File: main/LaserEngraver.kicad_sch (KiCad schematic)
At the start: 3 parts, among them J1 Conn_01x04_Socket, U1 STM32F103C8Tx

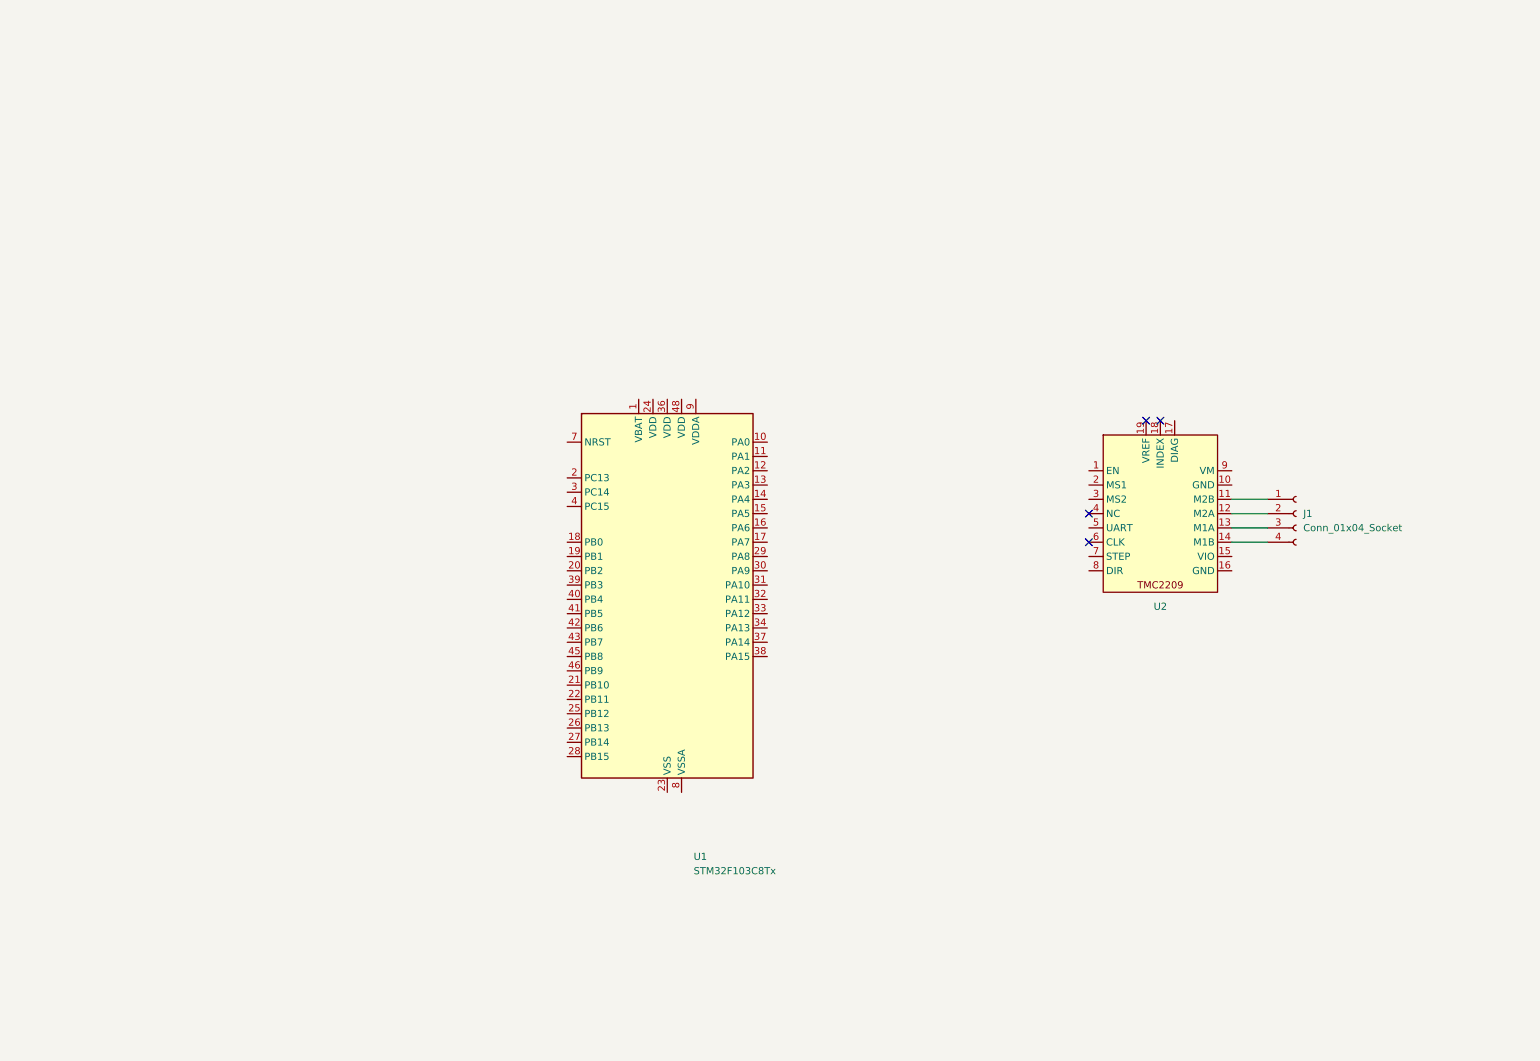
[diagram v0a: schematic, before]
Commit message: Made most connections between STM32 and motor drivers, as well as onboard connectors
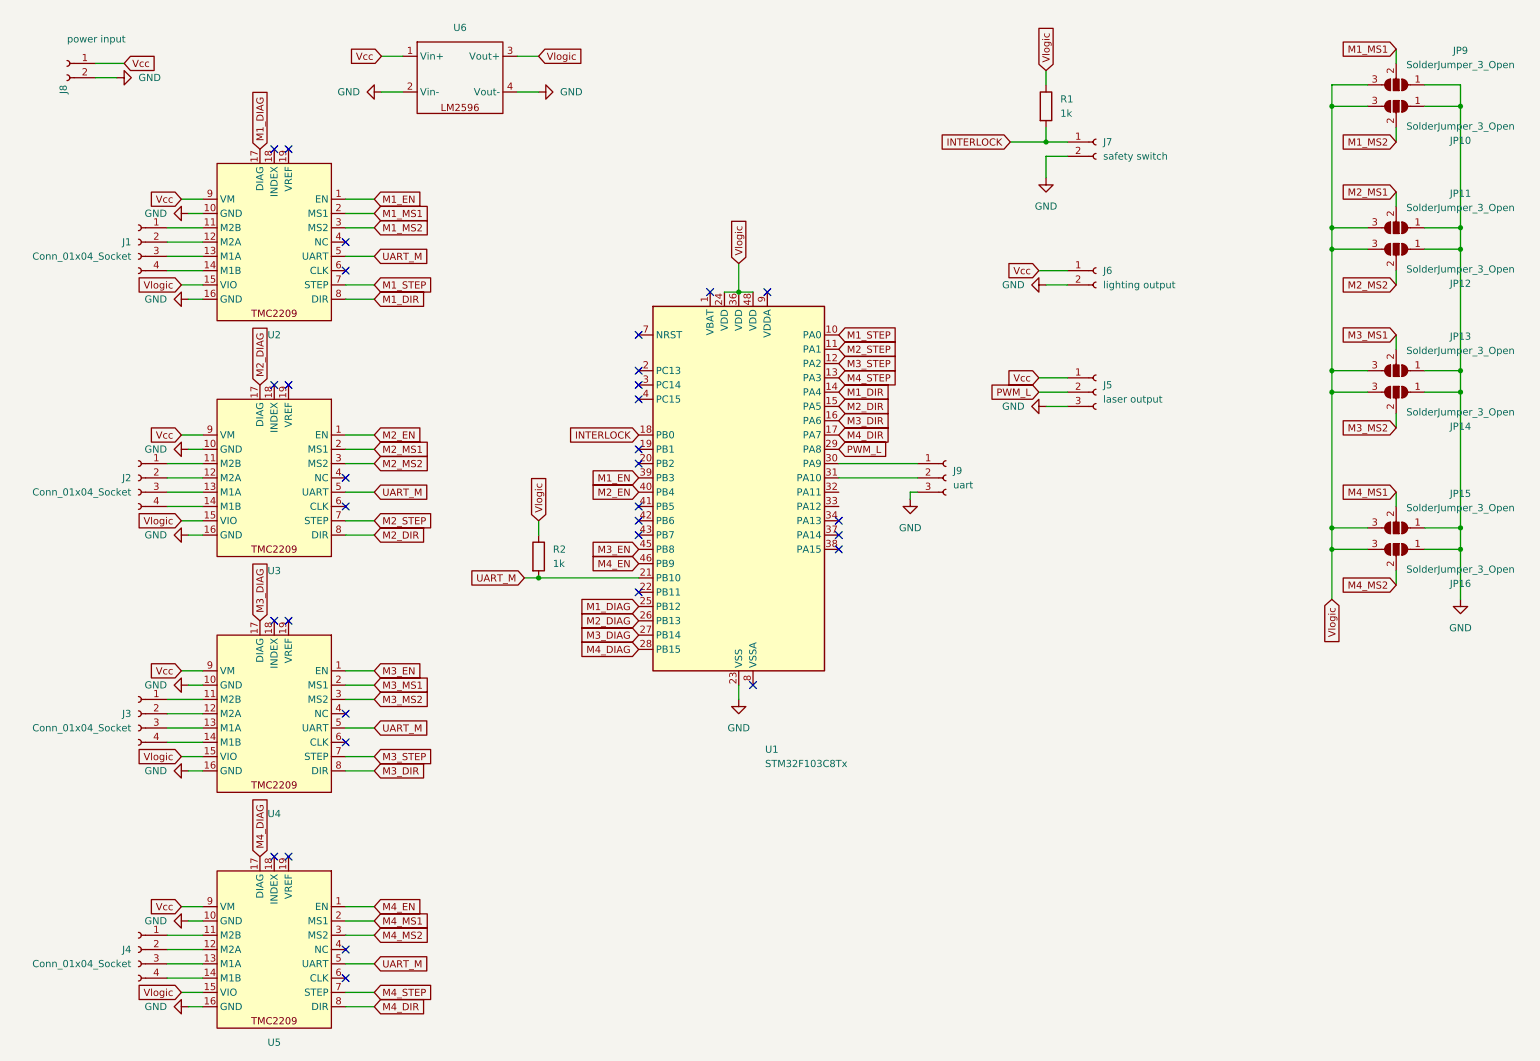
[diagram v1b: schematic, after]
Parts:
- added J2, J3, J4: Conn_01x04_Socket, symbol Connector:Conn_01x04_Socket
- added J5: laser output, symbol Connector:Conn_01x03_Socket
- added J6: lighting output, symbol Connector:Conn_01x02_Socket
- added J7: safety switch, symbol Connector:Conn_01x02_Socket
- added J8: power input, symbol Connector:Conn_01x02_Socket
- added J9: uart, symbol Connector:Conn_01x03_Socket
- added JP10, JP11, JP12, JP13, JP14, JP15, JP16, JP9: SolderJumper_3_Open, symbol Jumper:SolderJumper_3_Open
- added R1, R2: 1k, symbol Device:R
- added U3, U4, U5: (no value), symbol CustomSymbols:TMC2209
- added U6: (no value), symbol CustomSymbols:buck_converter_lm2596
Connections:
- net M1_EN: now reaches U2.1 (EN)
- net M1_EN: now also U1.39 (PB3)
- net GND: now reaches U2.10 (GND)
- net GND: now also U1.23 (VSS), U1.35 (VSS), U1.47 (VSS), U2.16 (GND), J5.3 (Pin_3), J6.2 (Pin_2), J7.2 (Pin_2), J8.2 (Pin_2), J9.3 (Pin_3), JP10.1 (A), JP11.1 (A), JP12.1 (A), JP13.1 (A), JP14.1 (A), JP15.1 (A), JP16.1 (A), JP9.1 (A), U3.10 (GND), U3.16 (GND), U4.10 (GND), U4.16 (GND), U5.10 (GND), U5.16 (GND), U6.2 (Vin-), U6.4 (Vout-)
- net Vlogic: now reaches U2.15 (VIO)
- net Vlogic: now also U1.24 (VDD), U1.36 (VDD), U1.48 (VDD), JP10.3 (B), JP11.3 (B), JP12.3 (B), JP13.3 (B), JP14.3 (B), JP15.3 (B), JP16.3 (B), JP9.3 (B), R1.1, R2.1, U3.15 (VIO), U4.15 (VIO), U5.15 (VIO), U6.3 (Vout+)
- net M1_DIAG: now reaches U2.17 (DIAG)
- net M1_DIAG: now also U1.25 (PB12)
- net M1_MS1: now reaches U2.2 (MS1)
- net M1_MS1: now also JP9.2 (C)
- net M1_MS2: now reaches U2.3 (MS2)
- net M1_MS2: now also JP10.2 (C)
- net UART_M: now reaches U2.5 (UART)
- net UART_M: now also U1.21 (PB10), R2.2, U3.5 (UART), U4.5 (UART), U5.5 (UART)
- net M1_STEP: now reaches U2.7 (STEP)
- net M1_STEP: now also U1.10 (PA0)
- net M1_DIR: now reaches U2.8 (DIR)
- net M1_DIR: now also U1.14 (PA4)
- net Vcc: now reaches U2.9 (VM)
- net Vcc: now also J5.1 (Pin_1), J6.1 (Pin_1), J8.1 (Pin_1), U3.9 (VM), U4.9 (VM), U5.9 (VM), U6.1 (Vin+)
- net M2_STEP: now reaches U1.11 (PA1)
- net M2_STEP: now also U3.7 (STEP)
- net M3_STEP: now reaches U1.12 (PA2)
- net M3_STEP: now also U4.7 (STEP)
- net M4_STEP: now reaches U1.13 (PA3)
- net M4_STEP: now also U5.7 (STEP)
- net M2_DIR: now reaches U1.15 (PA5)
- net M2_DIR: now also U3.8 (DIR)
- net M3_DIR: now reaches U1.16 (PA6)
- net M3_DIR: now also U4.8 (DIR)
- net M4_DIR: now reaches U1.17 (PA7)
- net M4_DIR: now also U5.8 (DIR)
- net INTERLOCK: now reaches U1.18 (PB0)
- net INTERLOCK: now also J7.1 (Pin_1), R1.2
- net M2_DIAG: now reaches U1.26 (PB13)
- net M2_DIAG: now also U3.17 (DIAG)
- net M3_DIAG: now reaches U1.27 (PB14)
- net M3_DIAG: now also U4.17 (DIAG)
- net M4_DIAG: now reaches U1.28 (PB15)
- net M4_DIAG: now also U5.17 (DIAG)
- net PWM_L: now reaches U1.29 (PA8)
- net PWM_L: now also J5.2 (Pin_2)
- net at U1.30 (PA9): now also J9.1 (Pin_1)
- net at U1.31 (PA10): now also J9.2 (Pin_2)
- net M2_EN: now reaches U1.40 (PB4)
- net M2_EN: now also U3.1 (EN)
- net M3_EN: now reaches U1.45 (PB8)
- net M3_EN: now also U4.1 (EN)
- net M4_EN: now reaches U1.46 (PB9)
- net M4_EN: now also U5.1 (EN)
- new net: J3.1 (Pin_1), U4.11 (M2B)
- new net: J3.2 (Pin_2), U4.12 (M2A)
- new net: J3.3 (Pin_3), U4.13 (M1A)
- new net: J3.4 (Pin_4), U4.14 (M1B)
- new net: J2.1 (Pin_1), U3.11 (M2B)
- new net: J2.2 (Pin_2), U3.12 (M2A)
- new net: J2.3 (Pin_3), U3.13 (M1A)
- new net: J2.4 (Pin_4), U3.14 (M1B)
- new net: J4.1 (Pin_1), U5.11 (M2B)
- new net: J4.2 (Pin_2), U5.12 (M2A)
- new net: J4.3 (Pin_3), U5.13 (M1A)
- new net: J4.4 (Pin_4), U5.14 (M1B)
- new net M2_MS1: JP11.2 (C), U3.2 (MS1)
- new net M2_MS2: JP12.2 (C), U3.3 (MS2)
- new net M3_MS1: JP13.2 (C), U4.2 (MS1)
- new net M3_MS2: JP14.2 (C), U4.3 (MS2)
- new net M4_MS1: JP15.2 (C), U5.2 (MS1)
- new net M4_MS2: JP16.2 (C), U5.3 (MS2)
- no-connect marks 4 -> 32
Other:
- moved on the sheet: J1, U1, U2

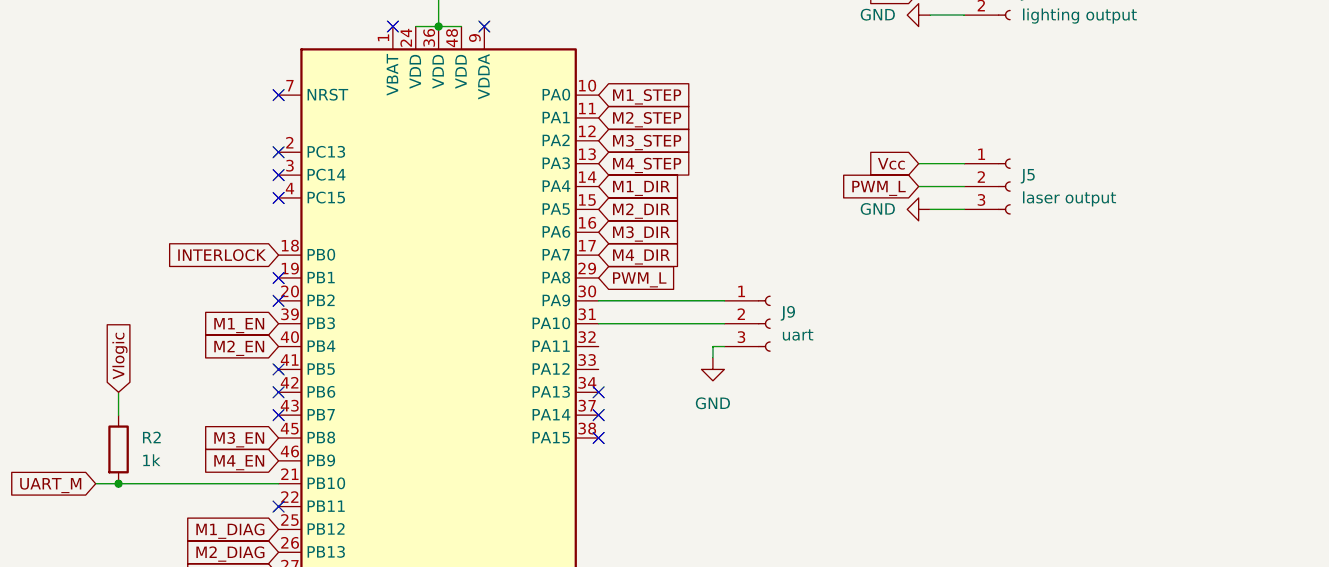
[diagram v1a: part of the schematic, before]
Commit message: Added fan connector and fan PWM connection
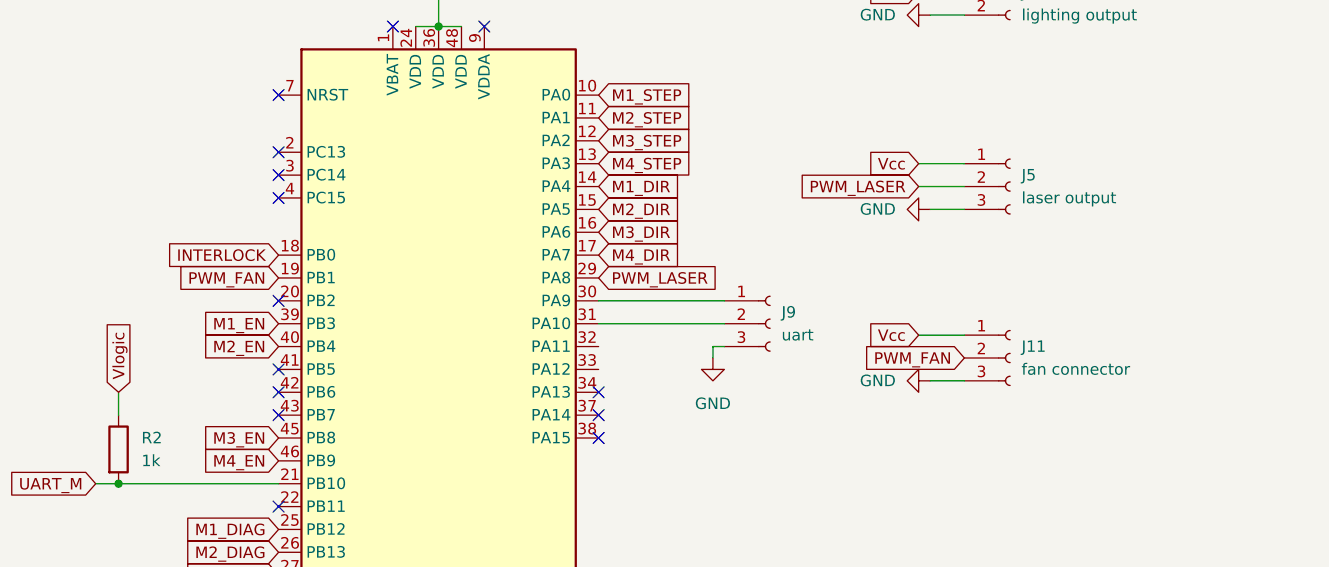
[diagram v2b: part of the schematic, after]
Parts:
- added J11: fan connector, symbol Connector:Conn_01x03_Socket
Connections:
- net GND: now also J11.3 (Pin_3)
- net Vcc: now also J11.1 (Pin_1)
- net PWM_FAN: now reaches U1.19 (PB1)
- net PWM_FAN: now also J11.2 (Pin_2)
- net PWM_L renamed PWM_LASER
- no-connect marks 32 -> 31
